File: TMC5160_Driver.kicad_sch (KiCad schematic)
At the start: 1 part, among them U4 TMC5160A-TA-T

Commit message: feat: connected necessary decoupling capacitors and resistor for external voltage regulation
Signed-off-by: Egor Shevchenko <egor.shevchenko.us@gmail.com>
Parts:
- added C25: 100n, Capacitor_SMD:C_0402_1005Metric, symbol Device:C
- added C26, C27: 2.2u, Capacitor_SMD:C_0402_1005Metric, symbol Device:C
- added C28: 470n, Capacitor_SMD:C_0402_1005Metric, symbol Device:C
- added R7: 2R2, symbol Device:R
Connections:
- net GND: now reaches U4.19 (GNDD)
- net GND: now also U4.6 (GNDA), C25.2, C26.2, C27.2, C28.2
- net vcc: now reaches U4.29 (VCC)
- net vcc: now also C28.1, R7.2
- net at U4.3 (12VOUT): now also C26.1
- net +12V_FUSED: now reaches U4.4 (VSA)
- net +12V_FUSED: now also C25.1
- net 5vout: now reaches U4.5 (5VOUT)
- net 5vout: now also C27.1, R7.1

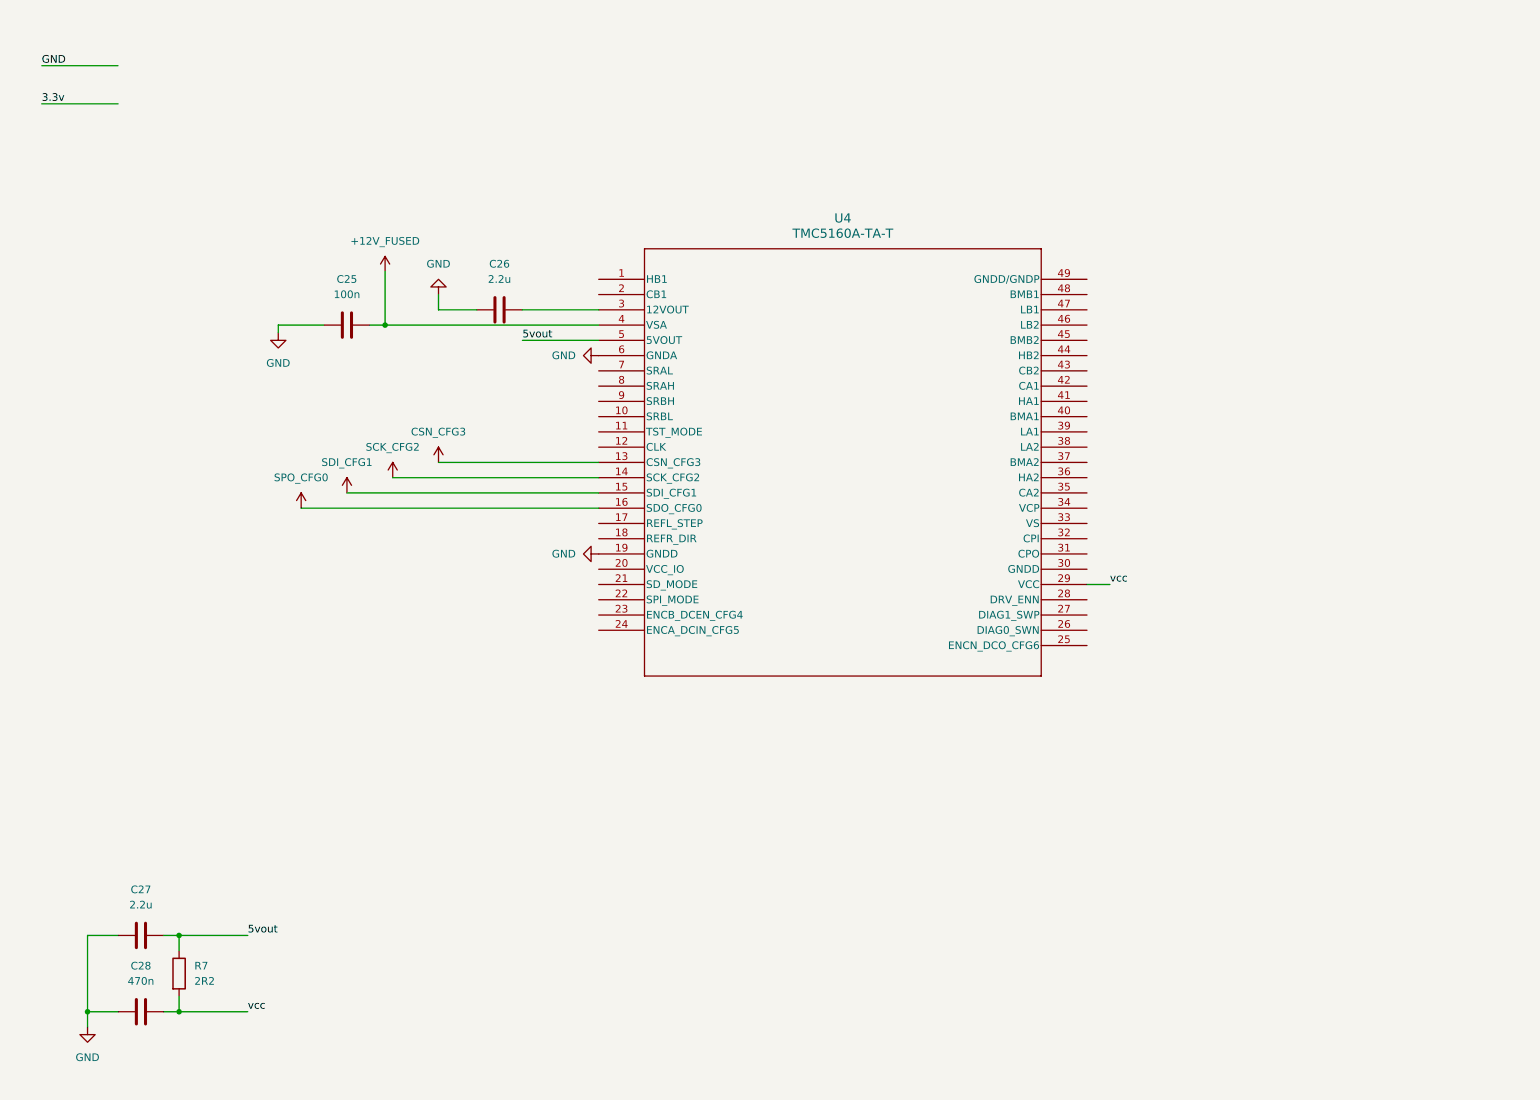
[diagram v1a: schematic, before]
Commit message: feat: connected vcc_io, VCP, VS, CPI, CPO
Signed-off-by: Egor Shevchenko <egor.shevchenko.us@gmail.com>
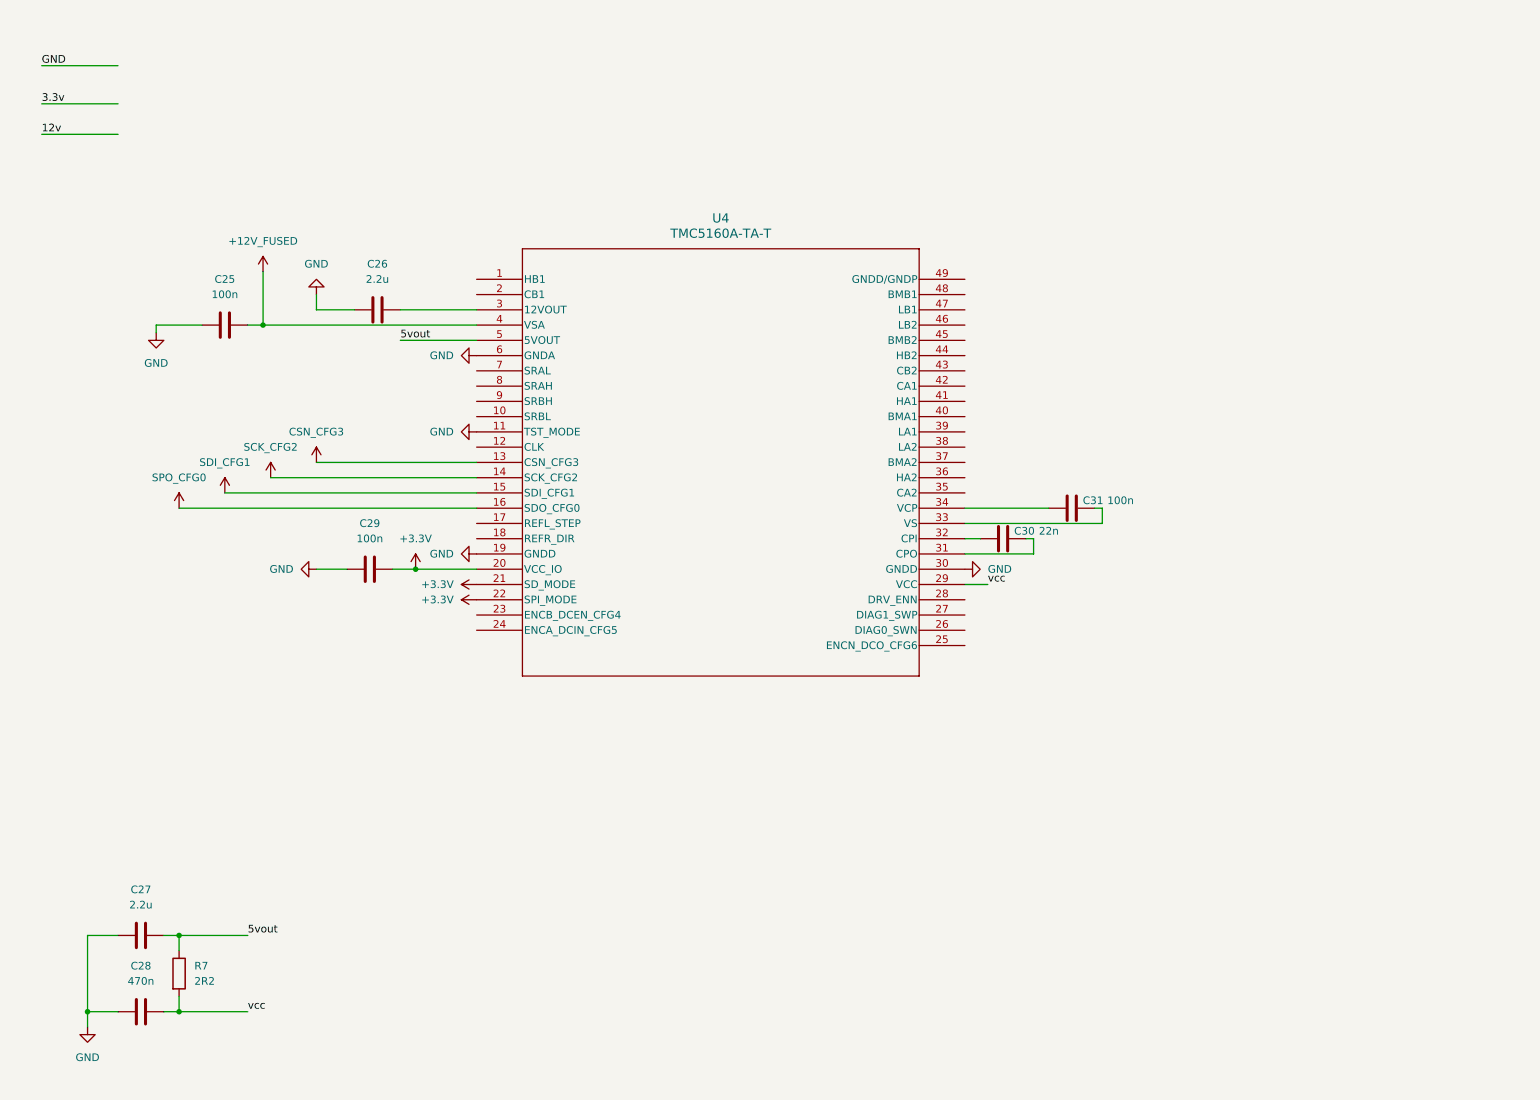
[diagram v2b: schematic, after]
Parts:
- added C29, C31: 100n, Capacitor_SMD:C_0402_1005Metric, symbol Device:C
- added C30: 22n, Capacitor_SMD:C_0402_1005Metric, symbol Device:C
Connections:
- net GND: now also U4.11 (TST_MODE), U4.30 (GNDD), C29.2
- net +3.3V: now reaches U4.20 (VCC_IO)
- net +3.3V: now also U4.21 (SD_MODE), U4.22 (SPI_MODE), C29.1
- net at U4.31 (CPO): now also C30.1
- net at U4.32 (CPI): now also C30.2
- net at U4.33 (VS): now also C31.1
- net at U4.34 (VCP): now also C31.2
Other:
- moved on the sheet: C25, C26, U4

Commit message: feat: designed the double H-bridge to drive a single stepper motor for a single tmc5160, pins DRV_ENN, REFL_STEP, REFL_DRV, etc. not wired yet
Signed-off-by: Egor Shevchenko <egor.shevchenko.us@gmail.com>
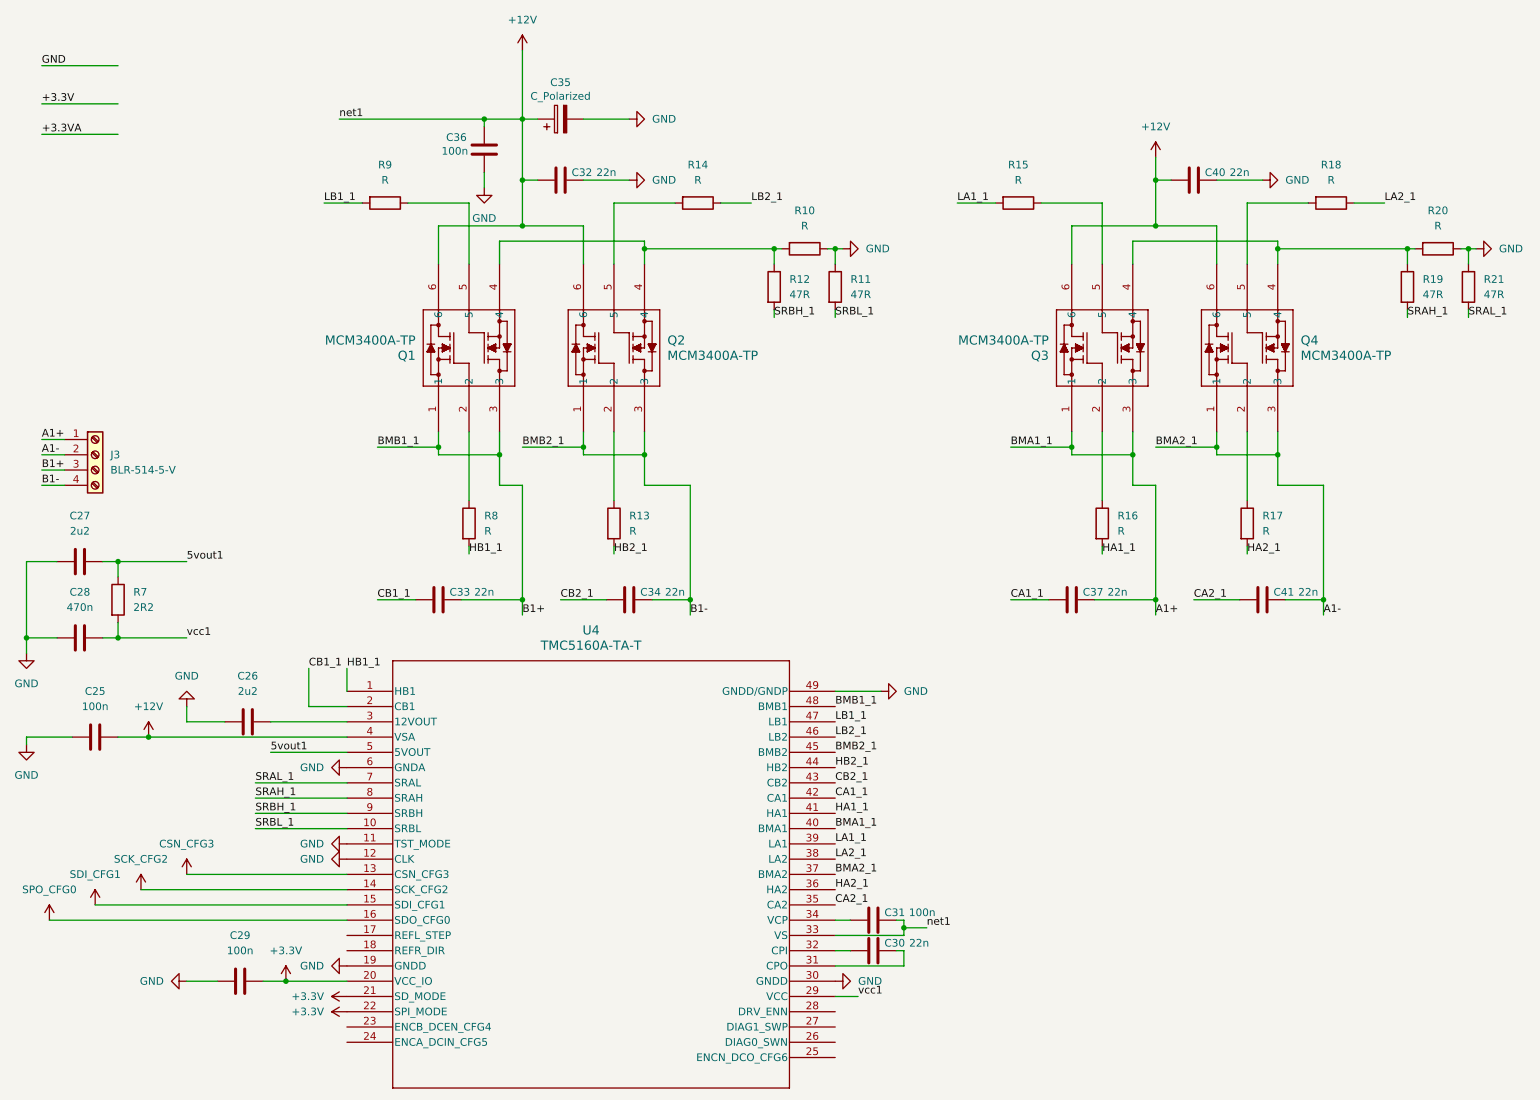
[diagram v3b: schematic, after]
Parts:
- added C32, C33, C34, C37, C40, C41: 22n, Capacitor_SMD:C_0402_1005Metric, symbol Device:C
- added C35: C_Polarized, symbol Device:C_Polarized
- added C36: 100n, Capacitor_SMD:C_0402_1005Metric, symbol Device:C
- added J3: BLR-514-5-V, symbol Connector:Screw_Terminal_01x04
- added Q1, Q2, Q3, Q4: MCM3400A-TP, DFN2020-6L_MCE, symbol Stepper_ESC:MCM3400A-TP
- added R10, R13, R14, R15, R16, R17, R18, R20, R8, R9: R, symbol Device:R
- added R11, R12, R19, R21: 47R, symbol Device:R
- C26, C27: value 2.2u -> 2u2
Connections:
- net +12V_FUSED is gone; now on net +12V: C25.1, U4.4 (VSA)
- net GND: now also U4.12 (CLK), U4.49 (GNDD/GNDP), C32.1, C35.2, C36.2, C40.1, R10.1, R11.1, R20.1, R21.1
- net +12V: now reaches C31.1, U4.33 (VS)
- net +12V: now also C32.2, C35.1, C36.1, C40.2, Q1.6, Q2.6, Q3.6, Q4.6
- net HB1_1: now reaches U4.1 (HB1)
- net HB1_1: now also R8.2
- net SRBL_1: now reaches U4.10 (SRBL)
- net SRBL_1: now also R11.2
- net CB1_1: now reaches U4.2 (CB1)
- net CB1_1: now also C33.2
- net CA2_1: now reaches U4.35 (CA2)
- net CA2_1: now also C41.2
- net HA2_1: now reaches U4.36 (HA2)
- net HA2_1: now also R17.2
- net A1-: now reaches U4.37 (BMA2)
- net A1-: now also C41.1, J3.2 (Pin_2), Q4.1, Q4.3
- net LA2_1: now reaches U4.38 (LA2)
- net LA2_1: now also R18.1
- net LA1_1: now reaches U4.39 (LA1)
- net LA1_1: now also R15.2
- net A1+: now reaches U4.40 (BMA1)
- net A1+: now also C37.1, J3.1 (Pin_1), Q3.1, Q3.3
- net HA1_1: now reaches U4.41 (HA1)
- net HA1_1: now also R16.2
- net CA1_1: now reaches U4.42 (CA1)
- net CA1_1: now also C37.2
- net CB2_1: now reaches U4.43 (CB2)
- net CB2_1: now also C34.2
- net HB2_1: now reaches U4.44 (HB2)
- net HB2_1: now also R13.2
- net B1-: now reaches U4.45 (BMB2)
- net B1-: now also C34.1, J3.4 (Pin_4), Q2.1, Q2.3
- net LB2_1: now reaches U4.46 (LB2)
- net LB2_1: now also R14.1
- net LB1_1: now reaches U4.47 (LB1)
- net LB1_1: now also R9.2
- net B1+: now reaches U4.48 (BMB1)
- net B1+: now also C33.1, J3.3 (Pin_3), Q1.1, Q1.3
- net SRAL_1: now reaches U4.7 (SRAL)
- net SRAL_1: now also R21.2
- net SRAH_1: now reaches U4.8 (SRAH)
- net SRAH_1: now also R19.2
- net SRBH_1: now reaches U4.9 (SRBH)
- net SRBH_1: now also R12.2
- net 5vout renamed 5vout1
- net vcc renamed vcc1
- new net: Q1.4, Q2.4, R10.2, R12.1
- new net: Q3.4, Q4.4, R19.1, R20.2
- new net: Q3.2, R16.1
- new net: Q2.5, R14.2
- new net: Q4.5, R18.2
- new net: Q4.2, R17.1
- new net: Q3.5, R15.1
- new net: Q1.5, R9.1
- new net: Q2.2, R13.1
- new net: Q1.2, R8.1
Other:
- moved on the sheet: C25, C26, C27, C28, C29, C30, C31, R7, U4

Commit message: feat: changed resistor value labels to match RKM notation, changed resistor and capacitor values of H-Birdges, set communication pin labels to hierarchical labels
Signed-off-by: Egor Shevchenko <egor.shevchenko.us@gmail.com>
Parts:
- C33, C34, C37, C41: value 22n -> 100n
- C35: value C_Polarized -> 2n2
- R10, R20: value R -> 75m
- R11, R12, R19, R21: value 47R -> 47
- R13, R14, R15, R16, R17, R18, R8, R9: value R -> 10
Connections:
- net SPO_CFG0 renamed SDO_CFG0
